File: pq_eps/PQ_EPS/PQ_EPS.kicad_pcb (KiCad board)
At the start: 4 copper layers, 40 x 40 mm, 86 parts, among them IC1 DS2782E+, IC2 ISL9120IRTNZ, J1 SLW-110-01-T-S, J2 SLW-110-01-T-S, J4 SLW-110-01-T-S, U1 SPV1040TTR, U2 SPV1040TTR, U3 SPV1040TTR, U4 LTC4040EUFD#PBF

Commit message: fabrication
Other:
- board text added: "+X"
- board text added: "+Z"
- board text added: "-X"
- board text added: "-Z"
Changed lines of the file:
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@@
     (effects (font (size 1.5 1.5) (thickness 0.15)) (justify left))
+  )
+  (gr_text "-X" (at 127.788 57.878) (layer "Cmts.User")
+    (effects (font (size 1 1) (thickness 0.15)) (justify left bottom))
+  )
+  (gr_text "+Z" (at 99.888 33.078) (layer "Cmts.User")
+    (effects (font (size 1 1) (thickness 0.15)) (justify left bottom))
+  )
+  (gr_text "-Z" (at 101.088 85.578) (layer "Cmts.User")
+    (effects (font (size 1 1) (thickness 0.15)) (justify left bottom))
+  )
+  (gr_text "+X" (at 71.388 57.578) (layer "Cmts.User")
+    (effects (font (size 1 1) (thickness 0.15)) (justify left bottom))
   )
   (segment (start 108.4 47) (end 108.4 48.7) (width 0.25) (layer "F.Cu") (net 1))

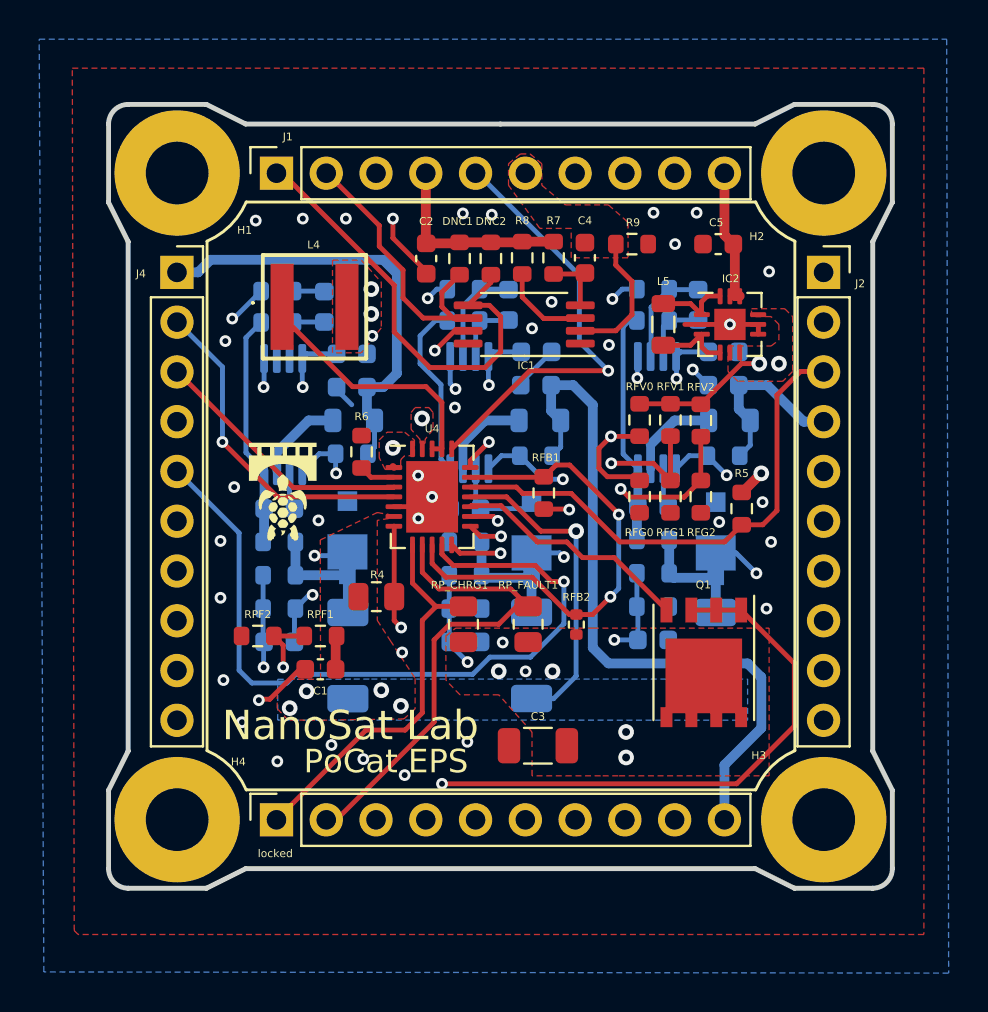
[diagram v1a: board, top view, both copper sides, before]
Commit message: J4 pin was inversed, and traces connected wrongly. Now it is correct. Reorder is needed. F in chat
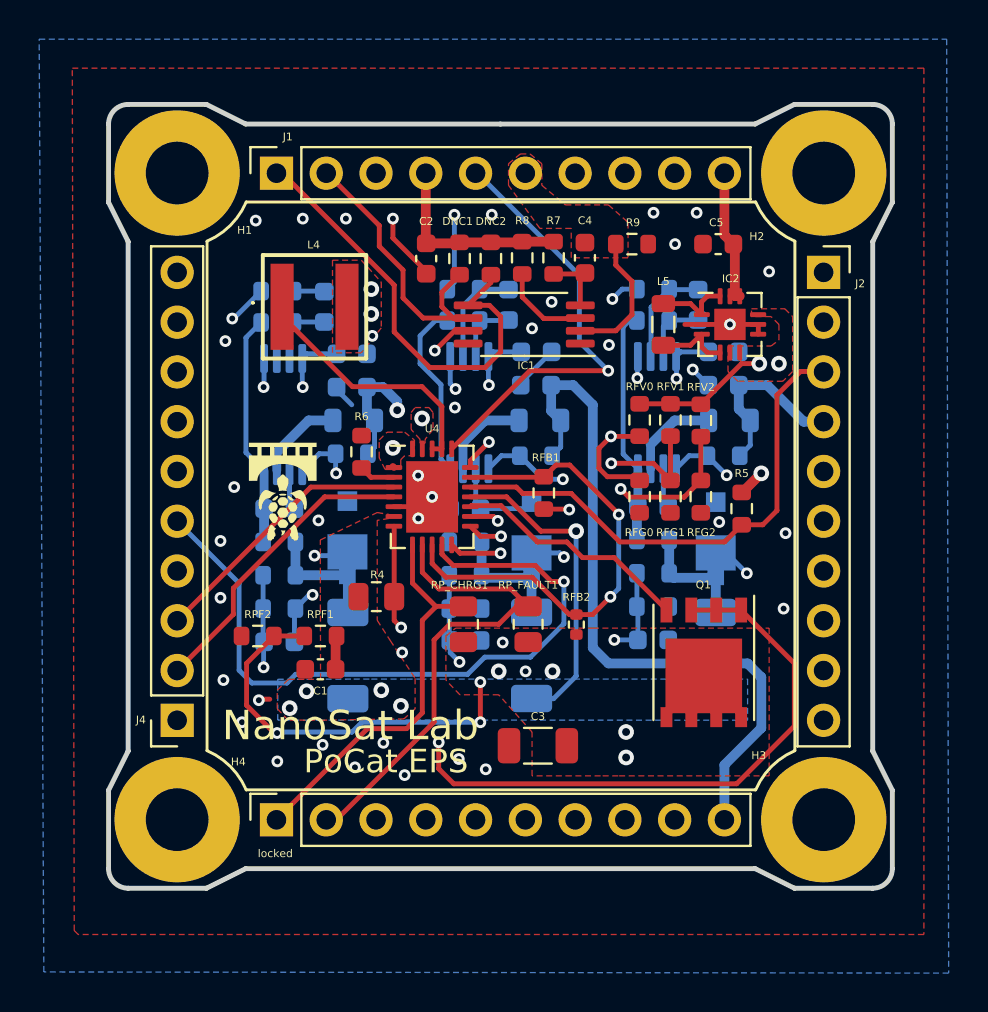
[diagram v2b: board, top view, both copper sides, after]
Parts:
- moved J4 22.9 mm to (85.2, 69.4), turned to 180 degrees
- moved COUTSNS3 0.07 mm to (99.9, 65.3)
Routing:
- net Net-(U4-PFI): track 25.5 -> 35.0 mm, vias 2 -> 4
- net Net-(D3-Pad1): track 27.8 -> 35.1 mm
- net /SOLAR_X: track 22.4 -> 28.9 mm, vias 0 -> 1
- net /RST: track 39.0 -> 36.4 mm
- net GND: track 32.5 -> 30.3 mm
- net Net-(U3-VCTRL): track 23.1 -> 21.3 mm
- net /CHGOFF: track 17.0 -> 15.5 mm, vias 1 -> 0
- net Net-(U4-CLN): track 44.9 -> 45.6 mm
- net Net-(D2-Pad1): track 26.9 -> 26.3 mm

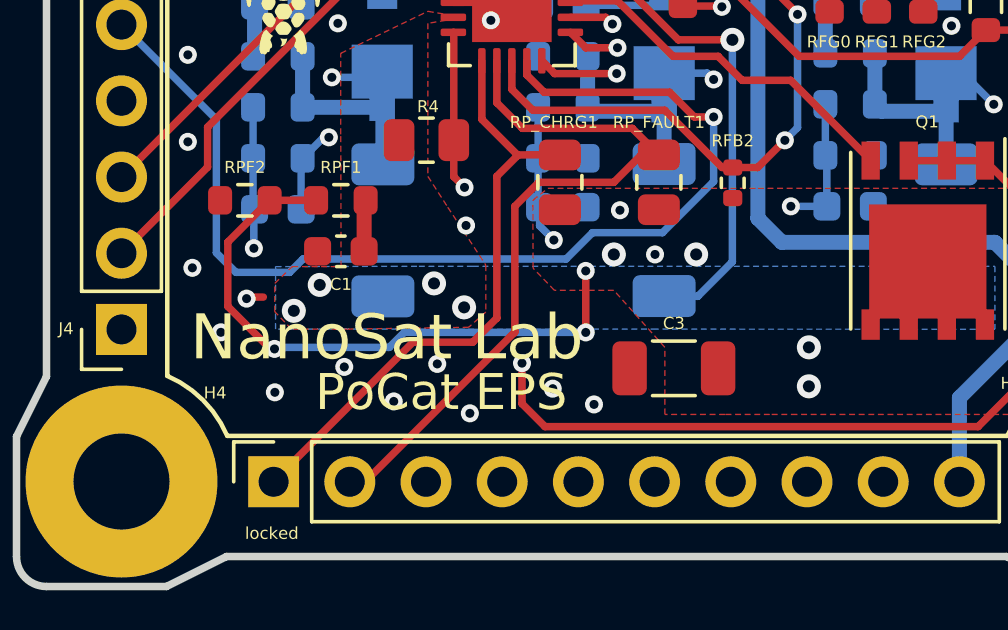
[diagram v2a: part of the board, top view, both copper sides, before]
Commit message: Added MPPT input pin for testing on board of the EGSE of the PQ nominal operation: Battery and MPPT input both in use
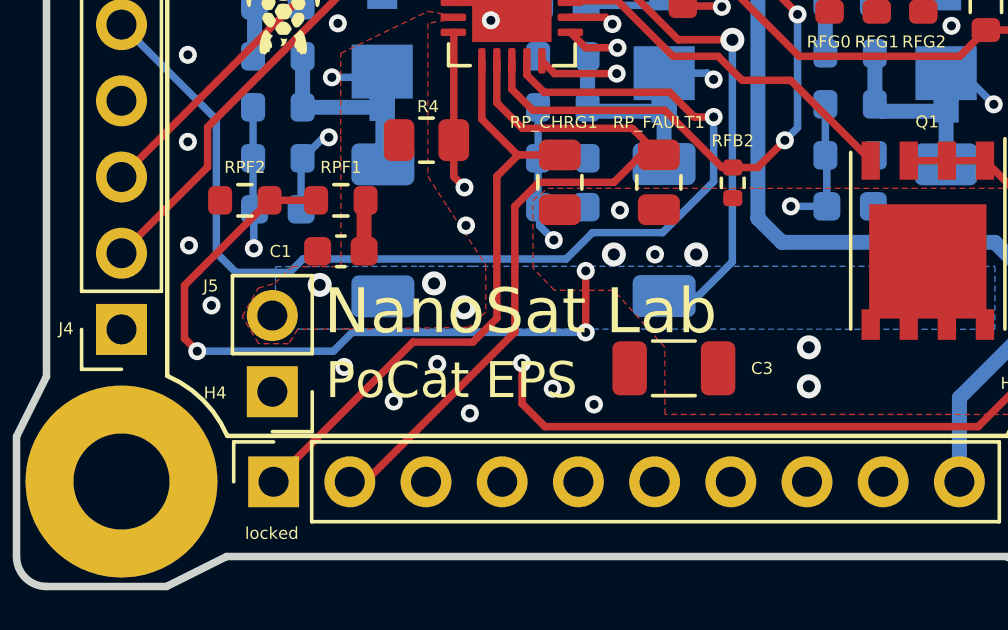
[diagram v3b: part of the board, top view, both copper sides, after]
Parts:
- added J5: ~, connector-nsl:CES-102-02, F.Cu at (90.2, 70.2)
- Q1: value ~ -> SIR424DP
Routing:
- net Net-(U4-PFI): track 35.0 -> 38.0 mm
- net GND: track 30.3 -> 29.8 mm, vias 43 -> 41
- net /OVSNS: vias 5 -> 4
